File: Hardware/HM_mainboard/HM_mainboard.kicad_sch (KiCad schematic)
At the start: 0 parts

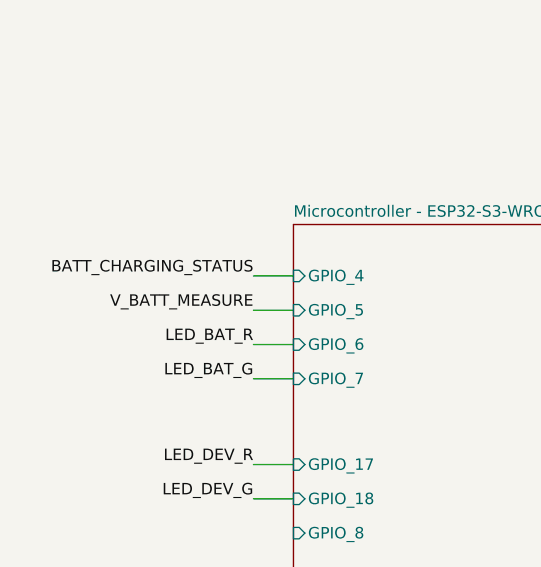
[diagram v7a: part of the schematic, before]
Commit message: Moved measurement lines. Updated PCB according to Aisler DRC
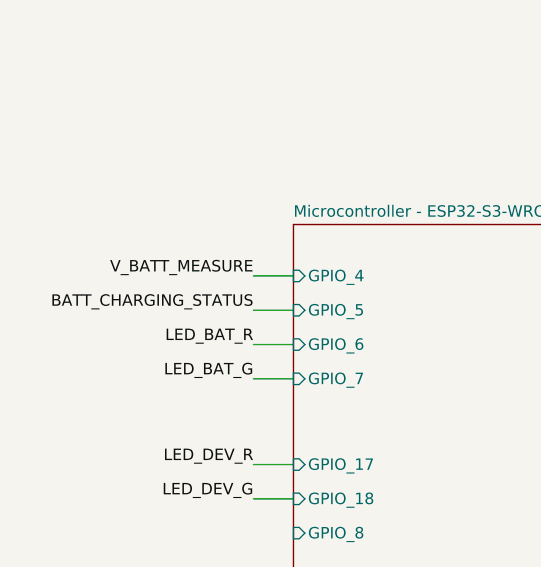
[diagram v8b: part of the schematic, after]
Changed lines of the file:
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@@
-    (stroke (width 0) (type default))
-  )
-  (wire (pts (xy 45.72 52.07) (xy 50.165 52.07))
     (stroke (width 0) (type default))
   )
@@
     (stroke (width 0) (type default))
   )
+  (wire (pts (xy 45.72 52.07) (xy 50.165 52.07))
+    (stroke (width 0) (type default))
+  )
   (wire (pts (xy 175.26 29.845) (xy 179.07 29.845))
     (stroke (width 0) (type default))
-  )
-  (label "BATT_CHARGING_STATUS" (at 45.72 48.26 180) (fields_autoplaced)
-    (effects (font (size 1.27 1.27)) (justify right bottom))
   )
   (label "LED_DEV_R" (at 45.72 69.215 180) (fields_autoplaced)
     (effects (font (size 1.27 1.27)) (justify right bottom))
   )
-  (label "V_BATT_MEASURE" (at 45.72 52.07 180) (fields_autoplaced)
+  (label "V_BATT_MEASURE" (at 45.72 48.26 180) (fields_autoplaced)
     (effects (font (size 1.27 1.27)) (justify right bottom))
   )
@@
     (effects (font (size 1.27 1.27)) (justify right bottom))
   )
+  (label "BATT_CHARGING_STATUS" (at 45.72 52.07 180) (fields_autoplaced)
+    (effects (font (size 1.27 1.27)) (justify right bottom))
+  )
